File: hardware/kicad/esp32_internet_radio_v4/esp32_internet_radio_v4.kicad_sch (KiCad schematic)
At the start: 17 parts, among them J1 ENCODER, J2 RGB LED, J3 ST7789, J4 extend, J5 POWER_IN_5V, J6 PCM5102, J7 TFT_SPI, P1 Power, P2 Analog, P3 Digital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

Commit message: update schematics
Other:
- note added: "ENCODER"
- note added: "ILI9488"
- note added: "PCM5102"
- note added: "POWER IN"
- note added: "RGB LED"
- note added: "ST7789"
- moved on the sheet: J7, R1, R2

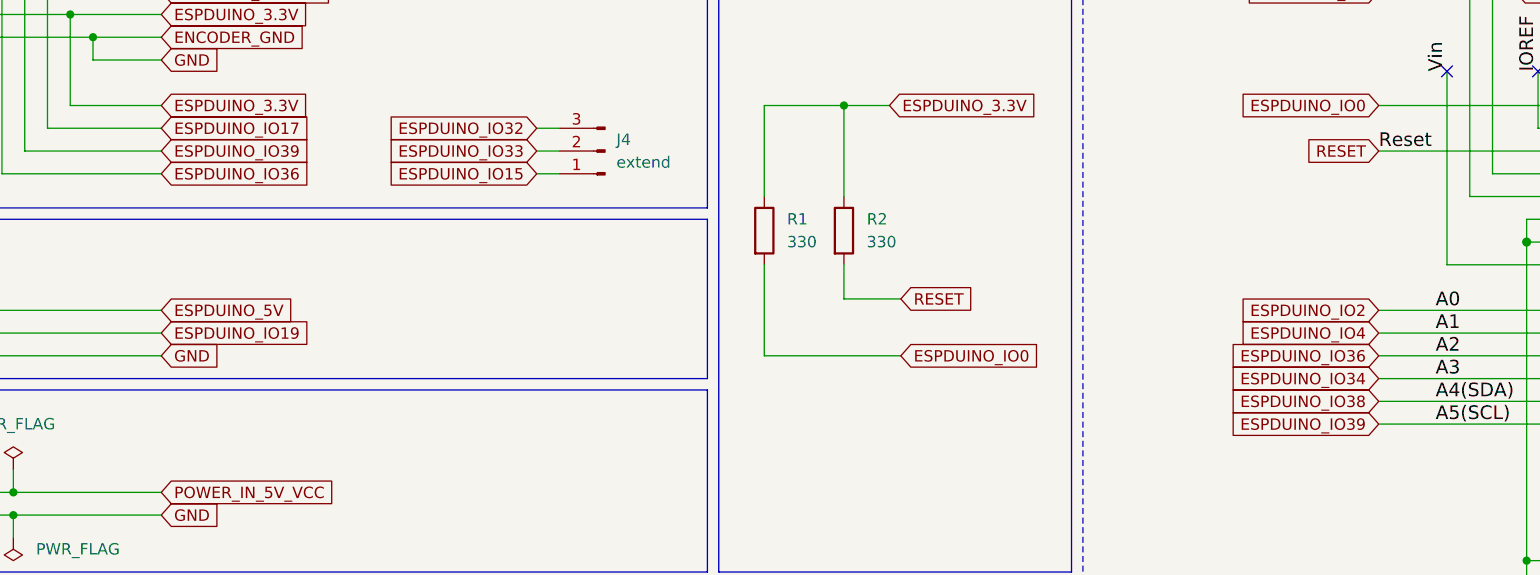
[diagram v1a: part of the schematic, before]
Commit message: update schematics (pinout)
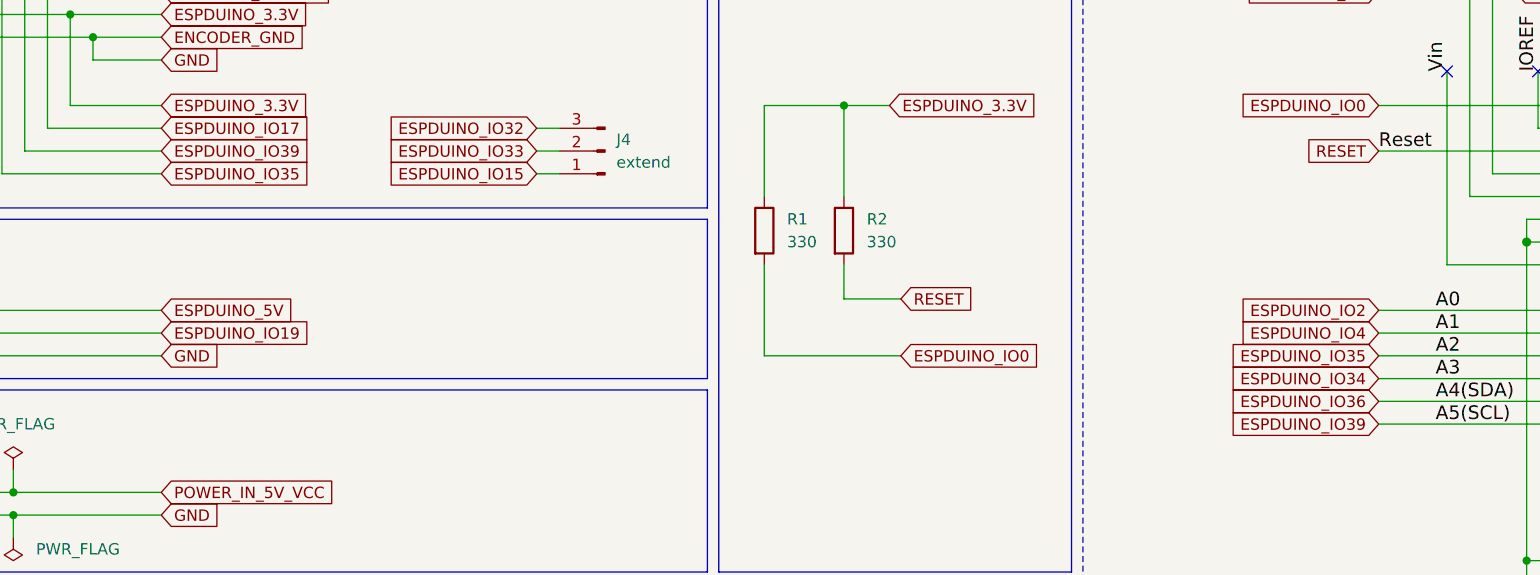
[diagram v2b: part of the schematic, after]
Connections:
- net ESPDUINO_IO38 renamed ESPDUINO_IO36
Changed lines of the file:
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@@
     )
   )
-  (global_label "ESPDUINO_IO38" (shape input) (at 190.5 73.66 180) (fields_autoplaced)
+  (global_label "ESPDUINO_IO36" (shape input) (at 190.5 73.66 180) (fields_autoplaced)
     (effects (font (size 1.27 1.27)) (justify right))
     (property "Intersheet References" "${INTERSHEET_REFS}" (id 0) (at 173.0797 73.5806 0)
@@
     )
   )
-  (global_label "ESPDUINO_IO36" (shape input) (at 190.5 68.58 180) (fields_autoplaced)
+  (global_label "ESPDUINO_IO35" (shape input) (at 190.5 68.58 180) (fields_autoplaced)
     (effects (font (size 1.27 1.27)) (justify right))
     (property "Intersheet References" "${INTERSHEET_REFS}" (id 0) (at 173.0797 68.5006 0)
@@
     )
   )
-  (global_label "ESPDUINO_IO36" (shape input) (at 54.61 48.26 0) (fields_autoplaced)
+  (global_label "ESPDUINO_IO35" (shape input) (at 54.61 48.26 0) (fields_autoplaced)
     (effects (font (size 1.27 1.27)) (justify left))
     (property "Intersheet References" "${INTERSHEET_REFS}" (id 0) (at 72.0303 48.1806 0)

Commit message: updated schematics and pcb
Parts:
- J1: footprint Connector_PinSocket_2.54mm:PinSocket_1x05_P2.54mm_Horizontal -> Connector_PinHeader_2.54mm:PinHeader_1x05_P2.54mm_Vertical
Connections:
- net ENCODER_DT: no longer P3.1 (Pin_1)
- net ESPDUINO_IO36: no longer P3.2 (Pin_2)
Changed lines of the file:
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@@
-    (effects (font (size 1.524 1.524)) (justify left bottom))
-  )
-  (label "A4(SDA)" (at 238.76 33.02 0)
     (effects (font (size 1.524 1.524)) (justify left bottom))
   )
@@
   )
   (label "8" (at 238.76 53.34 0)
-    (effects (font (size 1.524 1.524)) (justify left bottom))
-  )
-  (label "A5(SCL)" (at 238.76 30.48 0)
     (effects (font (size 1.524 1.524)) (justify left bottom))
   )
@@
     (property "Reference" "J1" (id 0) (at 28.575 17.78 0))
     (property "Value" "ENCODER" (id 1) (at 28.575 20.32 0))
-    (property "Footprint" "Connector_PinSocket_2.54mm:PinSocket_1x05_P2.54mm_Horizontal" (id 2) (at 27.94 27.94 0)
+    (property "Footprint" "Connector_PinHeader_2.54mm:PinHeader_1x05_P2.54mm_Vertical" (id 2) (at 27.94 27.94 0)
       (effects (font (size 1.27 1.27)) hide)
     )
@@
     )
     (path "/2a9e6e04-ecfe-4ea9-b7fb-b0b426c7e53b"
-      (reference "J1") (unit 1) (value "ENCODER") (footprint "Connector_PinSocket_2.54mm:PinSocket_1x05_P2.54mm_Horizontal")
+      (reference "J1") (unit 1) (value "ENCODER") (footprint "Connector_PinHeader_2.54mm:PinHeader_1x05_P2.54mm_Vertical")
     )
     (path "/ca9246e6-32c6-4653-9a63-7df8ea7c98df"

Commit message: update
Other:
- note added: "Wemos D1 R32 extension shield"
- note removed: "Shield for Arduino that uses the same pin disposition like "Uno" board Rev 3."
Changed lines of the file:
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@@
   (title_block
     (title "KEN ESP32 INTERNET RADIO HAT FOR ESPDUINO ")
-    (date "lun. 30 mars 2015")
+    (date "2022-06-21")
   )
   (junction (at 38.1 116.84) (diameter 0) (color 0 0 0 0)
@@
     (effects (font (size 1.524 1.524)) (justify left bottom))
   )
-  (text "Shield for Arduino that uses\nthe same pin disposition\nlike \"Uno\" board Rev 3."
-    (at 158.75 21.59 0)
+  (text "Wemos D1 R32 extension shield" (at 158.75 21.59 0)
     (effects (font (size 1.524 1.524)) (justify left bottom))
   )
